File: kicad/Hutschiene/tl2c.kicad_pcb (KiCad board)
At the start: 4 copper layers, 168.3 x 161.1 mm, 97 parts, among them IC101 ATTINY20-X, P101 12VDC, P102 I2C Master, P103 Spare, P104 TPI Header, P105 LED_DRIVER, P106 240VAC, P107 LED_DRIVER, P108 UG, P109 5VDC, P110 EG, P111 OG, P201 Mode_Bridge, P301 CONN_PIR_OG, P302 CONN_PIR_EG, P303 CONN_PIR_UG, Q301 IRLML2502, Q302 IRLML2502, Q303 IRLML2502, Q401 IRLML2502, Q402 IRLML2502, Q403 IRLML2502, SW101 TL3315NF160Q, U201 LF120ABDT-TR, U202 TPS70933

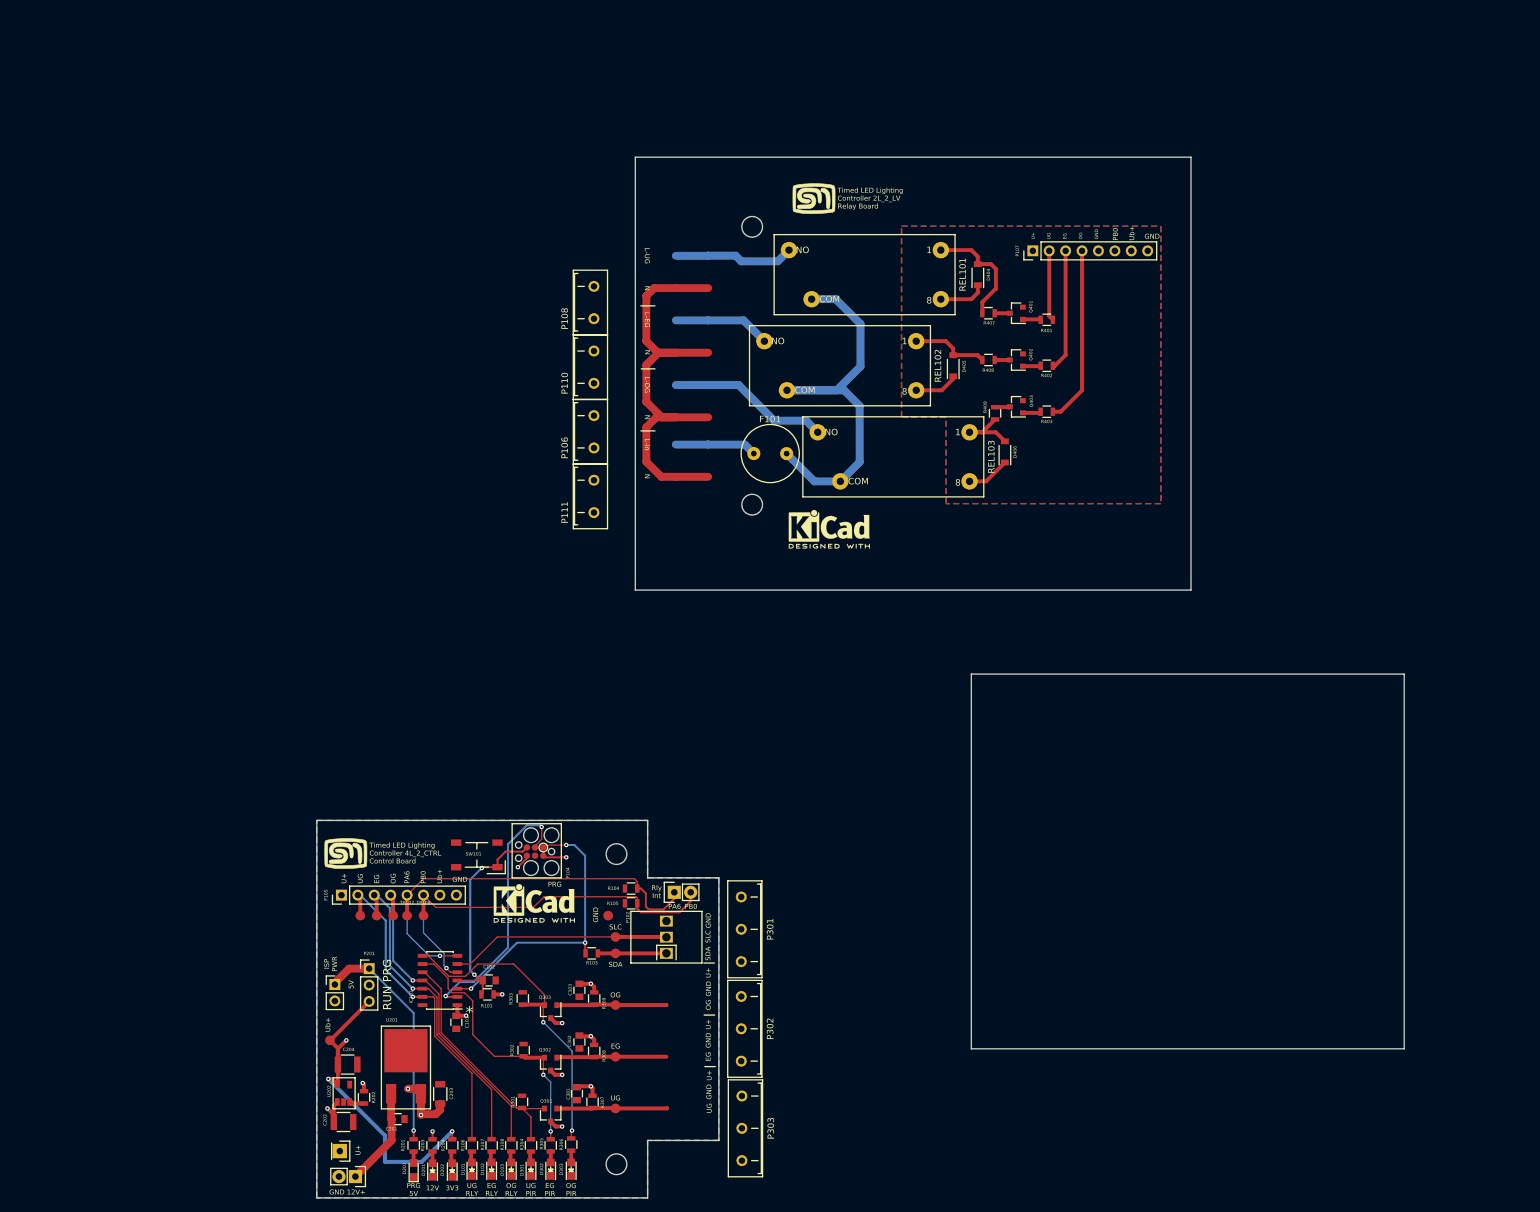
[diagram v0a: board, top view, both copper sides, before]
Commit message: Continuing with the Hutschiene design and layout
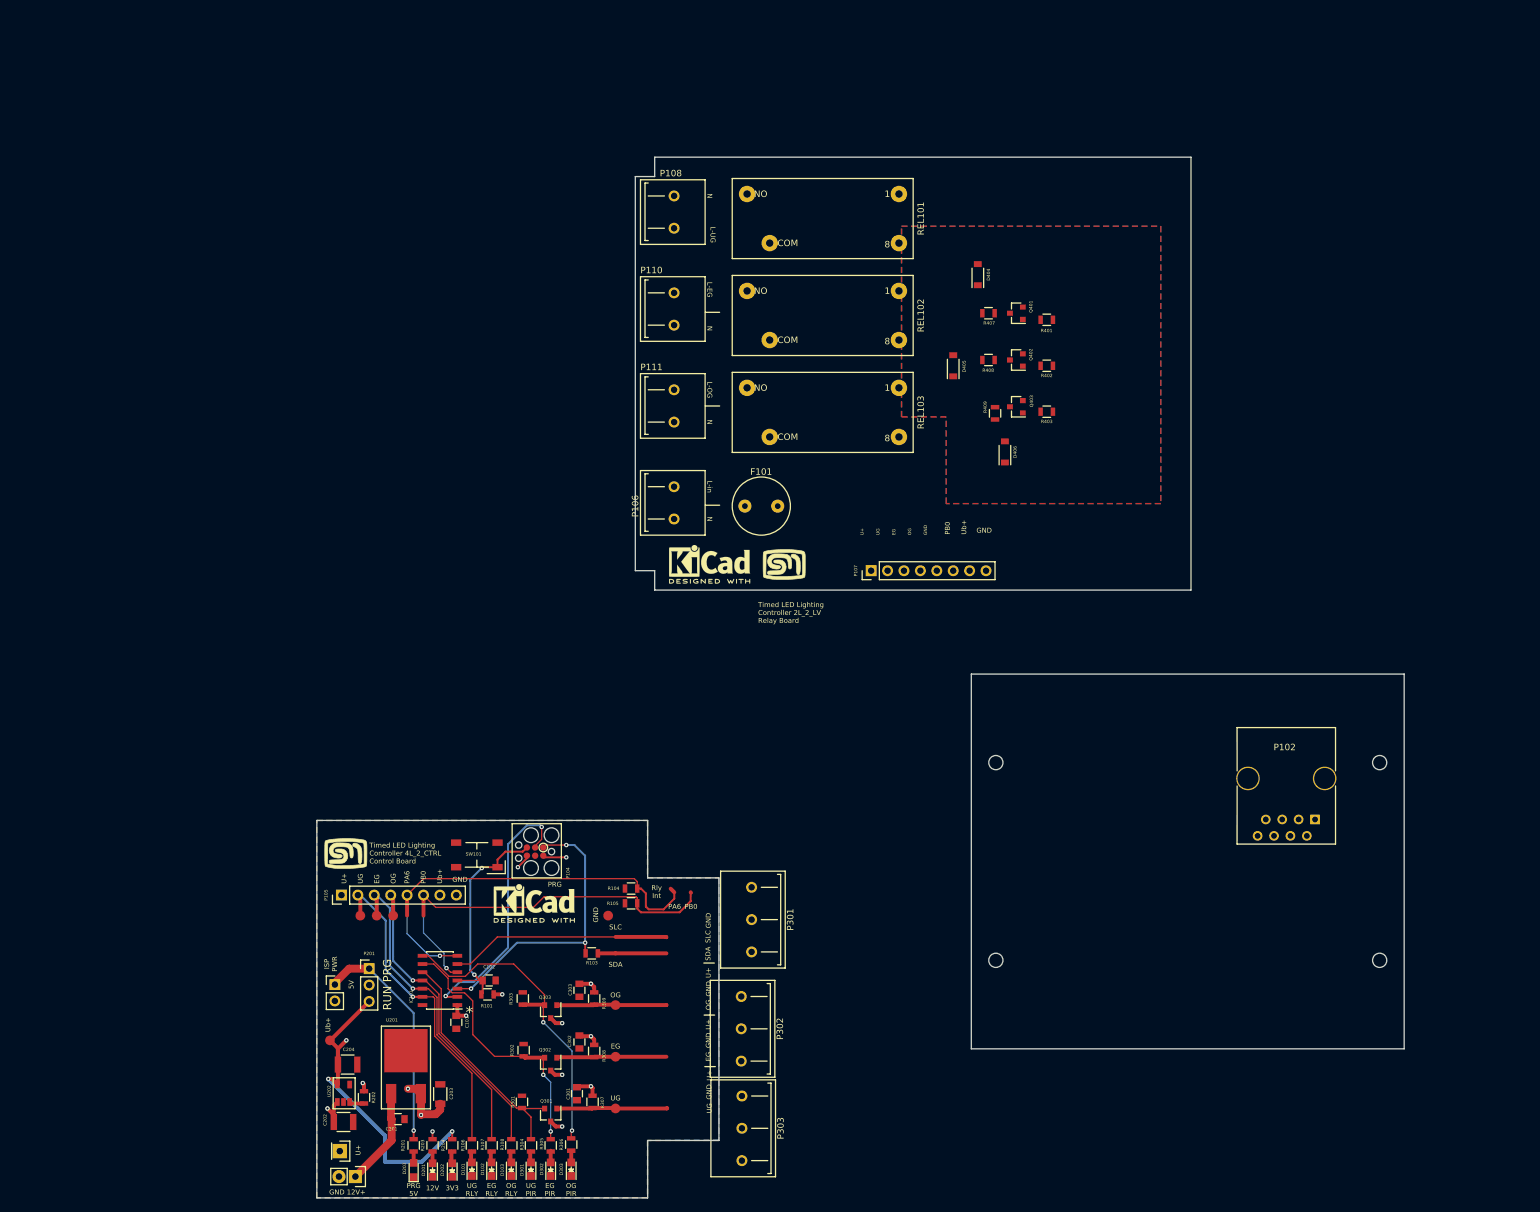
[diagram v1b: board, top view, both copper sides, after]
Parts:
- removed P103: Spare, Pin_Headers:Pin_Header_Straight_1x02
- removed REF** (x4): MountingHole_3.2mm_M3, Mounting_Holes:MountingHole_3.2mm_M3
- removed TP102: TPSCL, Measurement_Points:Measurement_Point_Round-SMD-Pad_Small
- removed TP103: TPSDA, Measurement_Points:Measurement_Point_Round-SMD-Pad_Small
- removed TP107: PA6, Measurement_Points:Measurement_Point_Round-SMD-Pad_Small
- removed TP108: PB0, Measurement_Points:Measurement_Point_Round-SMD-Pad_Small
- added MNT1: MountingHole_2.2mm_M2, Mounting_Holes:MountingHole_2.2mm_M2, F.Cu at (257.2, 142.3)
- added MNT1: MountingHole_2.2mm_M2, Mounting_Holes:MountingHole_2.2mm_M2, F.Cu at (257.2, 111.7)
- added MNT1: MountingHole_2.2mm_M2, Mounting_Holes:MountingHole_2.2mm_M2, F.Cu at (197.8, 142.3)
- added MNT1: MountingHole_2.2mm_M2, Mounting_Holes:MountingHole_2.2mm_M2, F.Cu at (197.8, 111.7)
- P102: value I2C Master -> RJ45; footprint tl2c-footprint:Spring_Terminal_Block_1_x_3 -> Connect:RJ45_8
- moved P102 102.5 mm to (247.2, 120.5)
- moved G*** 56.8 mm to (165.0, 81.0)
- moved P107 55.5 mm to (178.5, 82.0)
- moved REF*** 19.3 mm to (153.5, 81.0)
- moved P108 18.7 mm to (148.0, 24.0)
- moved P111 18.7 mm to (148.0, 54.0)
- moved P106 16.6 mm to (148.0, 69.0)
- moved P110 15.3 mm to (148.0, 39.0)
- moved REL103 12.9 mm to (171.0, 57.5)
- moved REL101 10.8 mm to (171.0, 27.5)
- moved F101 8.25 mm to (161.5, 72.0)
- moved REL102 8.23 mm to (171.0, 42.5)
- moved P301 2.19 mm to (160.0, 136.0)
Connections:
- IC101 pad 7: /GPIO_PA6 -> /RLY_INT
- P102 pad 1: /SDA -> GND
- P102 pad 2: /SCL -> /SDA
- P104 pad 4: Net-(P104-Pad4) -> (no net)
- P105 pad 5: /GPIO_PA6 -> (no net)
- P107 pad 5: Net-(P107-Pad5) -> (no net)
- P107 pad 6: Net-(P107-Pad6) -> (no net)
- P107 pad 7: Net-(P107-Pad7) -> (no net)
- R104 pad 2: /GPIO_PA6 -> /RLY_INT
- SW101 pad 2: Net-(SW101-Pad2) -> (no net)
- SW101 pad 4: Net-(SW101-Pad4) -> (no net)
- U202 pad 4: Net-(U202-Pad4) -> (no net)
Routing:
- net (no net): track 70.1 -> 0.56 mm
- net /RLY_INT: track 0.00 -> 67.9 mm, vias 0 -> 1
- net /GPIO_PA6: track 67.9 -> 0.00 mm, vias 1 -> 0
- net Net-(F101-Pad2): track 64.0 -> 0.00 mm
- net /LED Driver/Relay_OG: track 27.5 -> 0.00 mm
- net /LineOG: track 25.0 -> 0.00 mm
- net /LED Driver/LED_DRIVER_U+: track 20.7 -> 0.00 mm
- net /LED Driver/Relay_EG: track 18.8 -> 0.00 mm
- net /LineUG: track 18.6 -> 0.00 mm
- net Net-(D404-Pad2): track 18.0 -> 0.00 mm
- net /LineEG: track 15.3 -> 0.00 mm
- net /Lin: track 12.6 -> 0.00 mm
- net Net-(D405-Pad2): track 12.0 -> 0.00 mm
- net /LED Driver/Relay_UG: track 10.9 -> 0.00 mm
- net Net-(D406-Pad2): track 10.8 -> 0.00 mm
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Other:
- outline, holes or cut-outs redrawn

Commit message: Further work on the redesign
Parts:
- removed C301, C302, C303: 100nF 50V, Capacitors_SMD:C_0805
- removed D201: 12VDC, LEDs:LED_0805
- removed D301: LED__SIG_UG, LEDs:LED_0805
- removed D302: LED__SIG_EG, LEDs:LED_0805
- removed D303: LED__SIG_OG, LEDs:LED_0805
- removed the G*** at (165.0, 81.0)
- removed the MNT1 at (197.8, 111.7)
- removed P107: LED_DRIVER, Pin_Headers:Pin_Header_Straight_1x08_Pitch2.54mm
- removed P301: CONN_PIR_OG, tl2c-footprint:PCB_Screw_Terminal_Block_5mm_x_3
- removed P302: CONN_PIR_EG, tl2c-footprint:PCB_Screw_Terminal_Block_5mm_x_3
- removed P303: CONN_PIR_UG, tl2c-footprint:PCB_Screw_Terminal_Block_5mm_x_3
- removed R203: 2k4Ω, Resistors_SMD:R_0805
- removed R304, R305, R306: 660Ω, Resistors_SMD:R_0805
- removed the REF*** at (153.5, 81.0)
- added C501: 100nF 50V, Capacitors_SMD:C_0805, F.Cu at (216.3, 30.5)
- added C502: 100nF 50V, Capacitors_SMD:C_0805, F.Cu at (215.6, 69.0)
- added C503: 100nF 50V, Capacitors_SMD:C_0805, F.Cu at (215.4, 49.0)
- added P103: CTL CONN, Pin_Headers:Pin_Header_Straight_2x05_Pitch2.54mm, F.Cu at (243.0, 144.7)
- added P501: CONN_PIR_OG, tl2c-footprint:PCB_Screw_Terminal_Block_5mm_x_3, F.Cu at (222.5, 56.5)
- added P502: CONN_PIR_EG, tl2c-footprint:PCB_Screw_Terminal_Block_5mm_x_3, F.Cu at (222.5, 41.5)
- added P503: CONN_PIR_UG, tl2c-footprint:PCB_Screw_Terminal_Block_5mm_x_3, F.Cu at (222.5, 26.5)
- added REF**: MountingHole_2.2mm_M2, Mounting_Holes:MountingHole_2.2mm_M2, F.Cu at (197.8, 111.7)
- P101: footprint Pin_Headers:Pin_Header_Straight_1x02 -> tl2c-footprint:PCB_Screw_Terminal_Block_5mm_x_2
- P105: value LED_DRIVER -> DRV CONN; footprint Pin_Headers:Pin_Header_Straight_1x08_Pitch2.54mm -> Pin_Headers:Pin_Header_Straight_2x05_Pitch2.54mm
- moved P101 155.6 mm to (222.5, 81.5), turned to 90 degrees
- moved IC101 115.2 mm to (225.5, 127.3), turned to 90 degrees
- moved P105 112.8 mm to (197.9, 82.7)
- moved D103 110.7 mm to (229.0, 143.2)
- moved R108 110.7 mm to (229.0, 139.5)
- moved U201 110.0 mm to (207.4, 112.4)
- moved D102 108.8 mm to (224.0, 143.2)
- moved R107 108.8 mm to (224.0, 139.5)
- moved D101 107.0 mm to (219.0, 143.3)
- moved R106 107.0 mm to (219.0, 139.6)
- moved D203 106.1 mm to (209.0, 143.4)
- moved R201 106.1 mm to (209.0, 139.5)
- moved D202 105.1 mm to (214.0, 143.4)
- moved R204 105.1 mm to (214.0, 139.5)
- moved P104 72.1 mm to (198.6, 127.0)
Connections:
- P105 pad 1: /PIR13/U+ -> /LED Driver/LED_DRIVER_U+
- P105 pad 2: /RelayUG -> /LED Driver/Relay_UG
- P105 pad 3: /RelayEG -> /LED Driver/Relay_EG
- P105 pad 4: /RelayOG -> /LED Driver/Relay_OG
- P105 pad 5: (no net) -> /PIR13/Ub+
- P105 pad 6: /GPIO_PB2 -> (no net)
- P105 pad 7: /PIR13/Ub+ -> /PIR_Connector/PIR_OG
- P105 pad 8: GND -> /PIR_Connector/PIR_EG
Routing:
- net /RLY_INT: track 67.9 -> 0.00 mm, vias 1 -> 0
- net /GPIO_PB2: track 64.8 -> 0.00 mm, vias 1 -> 0
- net Net-(C204-Pad1): track 52.2 -> 0.00 mm, vias 3 -> 0
- net /PIR13/SIG_OG: track 50.6 -> 0.00 mm, vias 2 -> 0
- net /RelayUG: track 50.5 -> 0.00 mm, vias 1 -> 0
- net /RelayEG: track 50.2 -> 0.00 mm, vias 1 -> 0
- net /RelayOG: track 50.2 -> 0.00 mm, vias 1 -> 0
- net /TPIDATA: track 45.8 -> 0.00 mm, vias 3 -> 0
- net /PIR13/SIG_EG: track 42.2 -> 0.00 mm, vias 2 -> 0
- net /TPICLK: track 40.9 -> 0.00 mm, vias 2 -> 0
- net /PIR13/SIG_UG: track 38.1 -> 0.00 mm
- net /Power System/5V: track 35.7 -> 0.00 mm, vias 1 -> 0
- net /~Reset: track 34.3 -> 0.00 mm, vias 2 -> 0
- net /SCL: track 34.1 -> 0.00 mm
- net /PIR13/U+: track 29.0 -> 0.00 mm, vias 8 -> 0
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- removed copper zone on U+, net /PIR13/U+
- removed copper zone on Ub+, net /PIR13/Ub+
- removed copper zone on B.Cu, net GND
- removed copper zone on F.Cu, net GND
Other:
- board text removed: "12V"
- board text removed: "EG PIR"
- board text removed: "OG PIR"
- board text removed: "UG PIR"
